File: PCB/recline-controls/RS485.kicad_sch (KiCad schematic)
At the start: 16 parts, among them J3 RJHSE-5381, U3 MAX3535ECWI+T

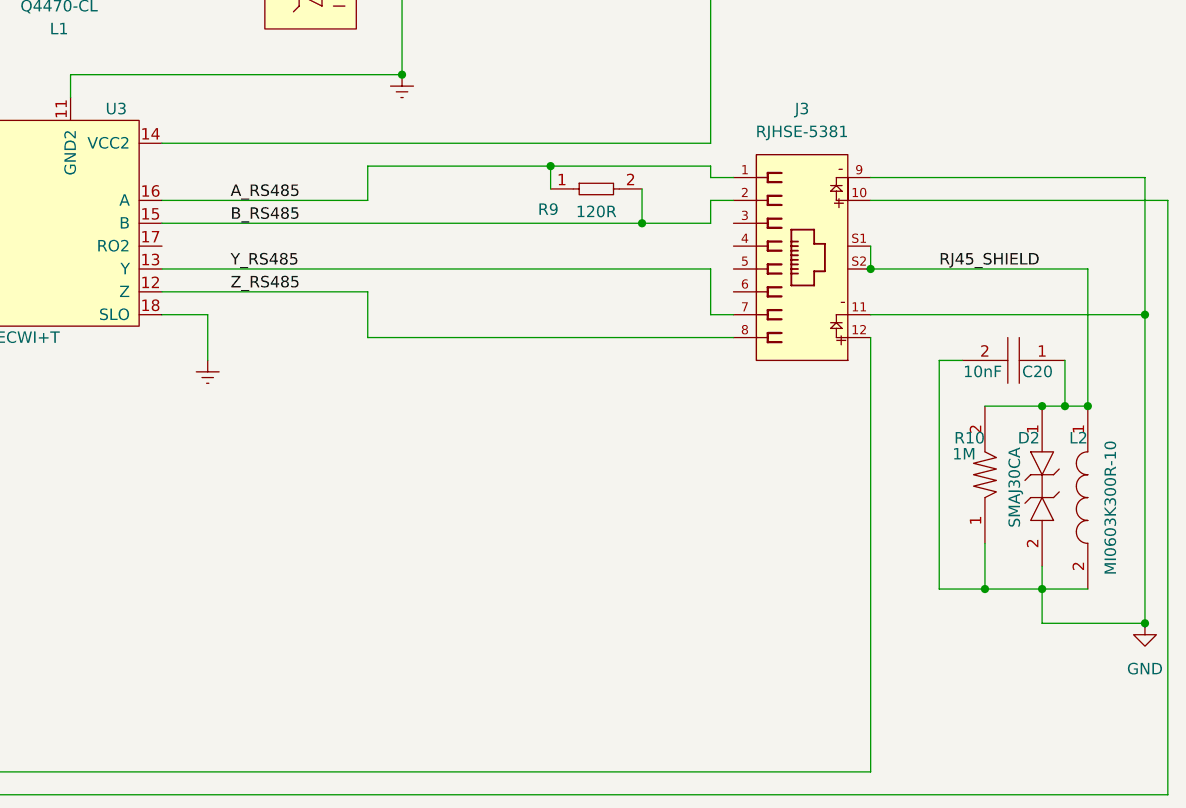
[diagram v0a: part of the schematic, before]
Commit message: HID
Changes made to recline control HID board. Power input section redesigned, 5V regulator removed, RS485 circuit updated with fixes that other boards received. Redesign or internal plane topology following changes to RS485 section. Via stitching all around.
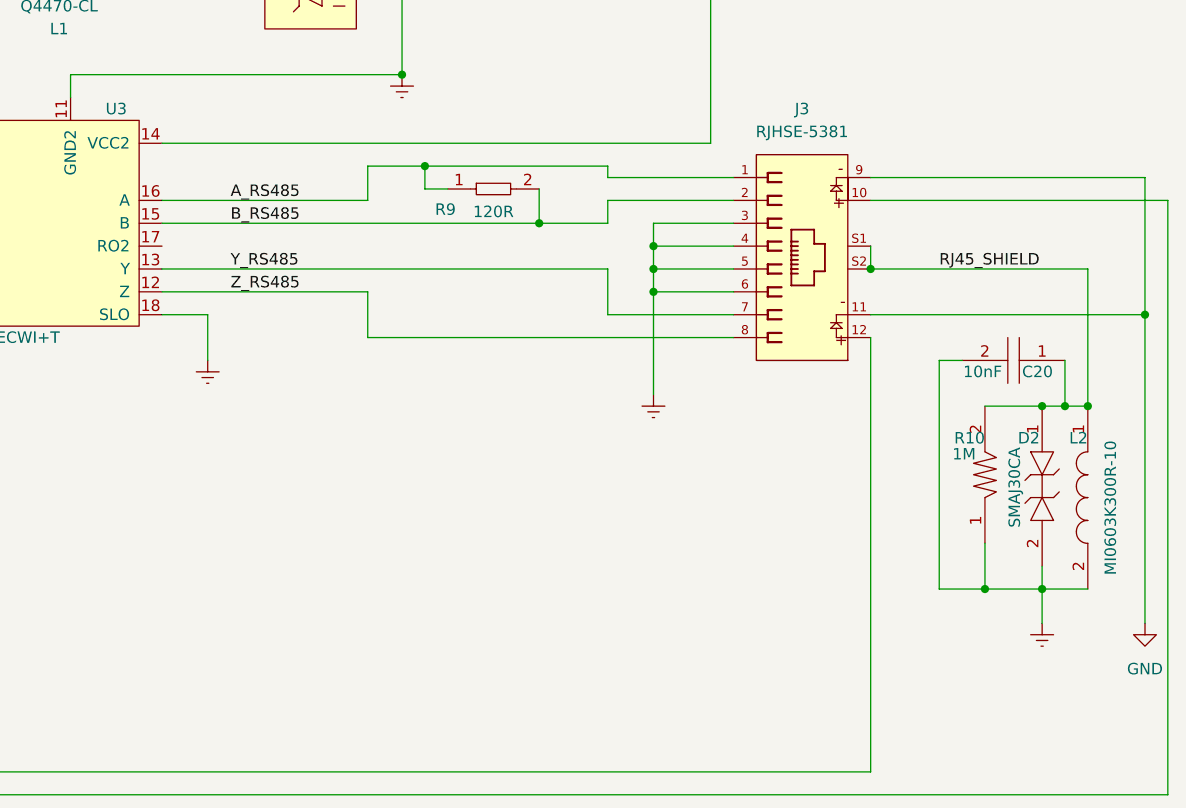
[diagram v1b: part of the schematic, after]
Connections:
- net Earth: now also C20.2, D2.2, J3.3, J3.4, J3.5, J3.6, L2.2, R10.1
- net GND: no longer C20.2, D2.2, L2.2, R10.1
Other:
- moved on the sheet: R9
